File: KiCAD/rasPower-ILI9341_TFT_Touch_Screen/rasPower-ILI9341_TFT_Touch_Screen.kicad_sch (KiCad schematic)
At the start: 2 parts, among them J1 Raspberry_Pi_2_3, U2 ST7735_1.8"_TFT_128x160_w_SD-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

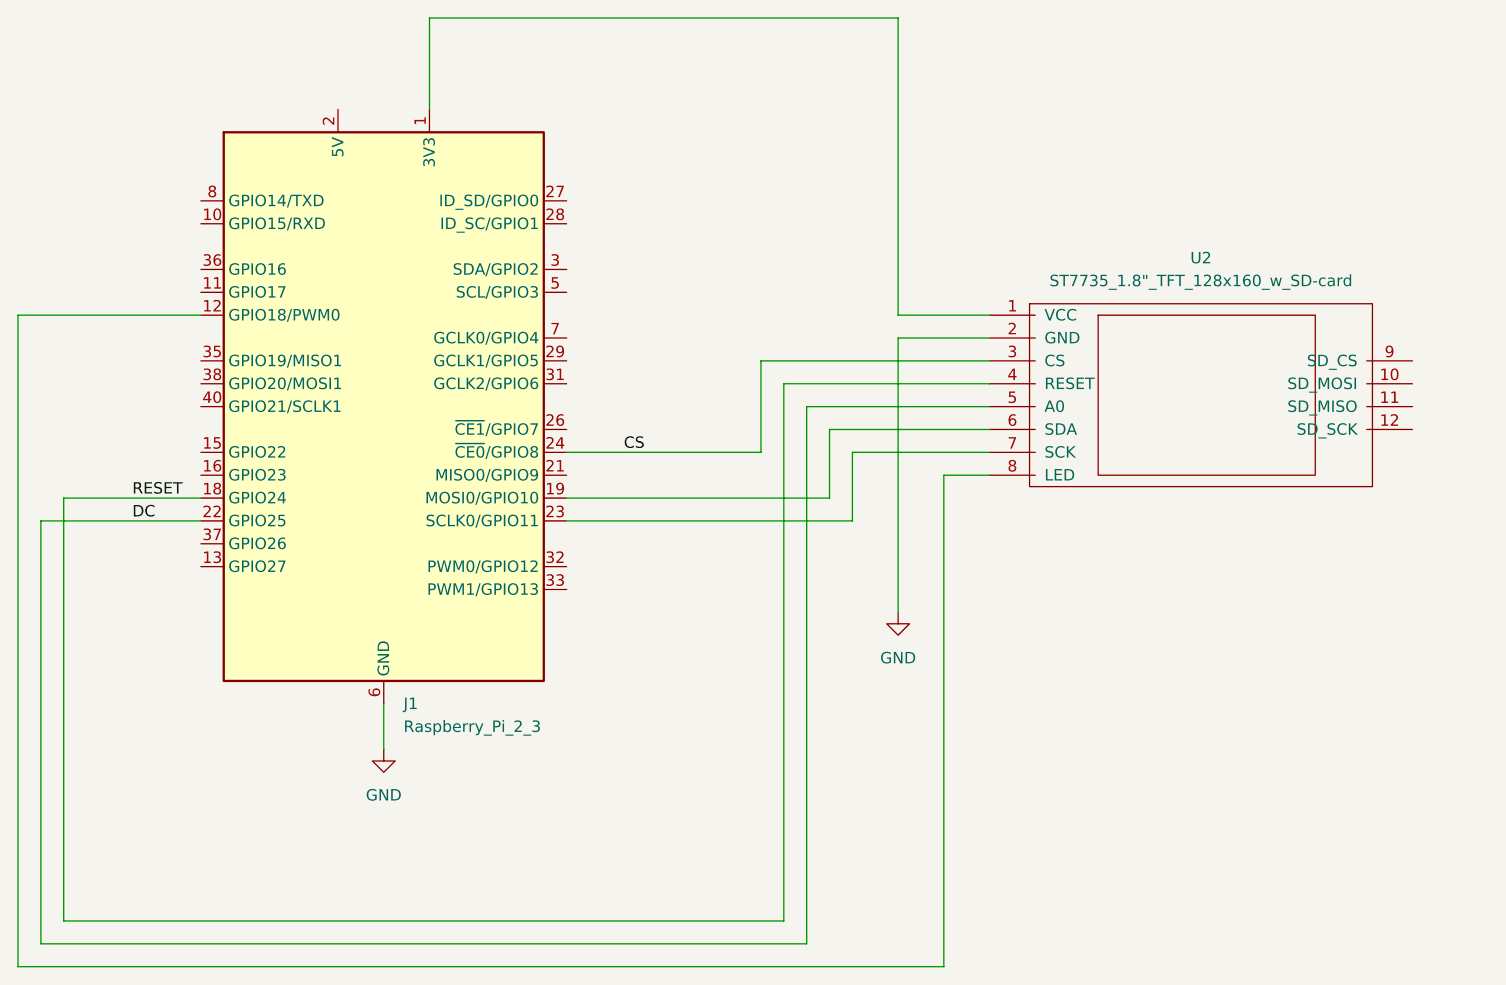
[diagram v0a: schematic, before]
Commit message: new ili9341 screen
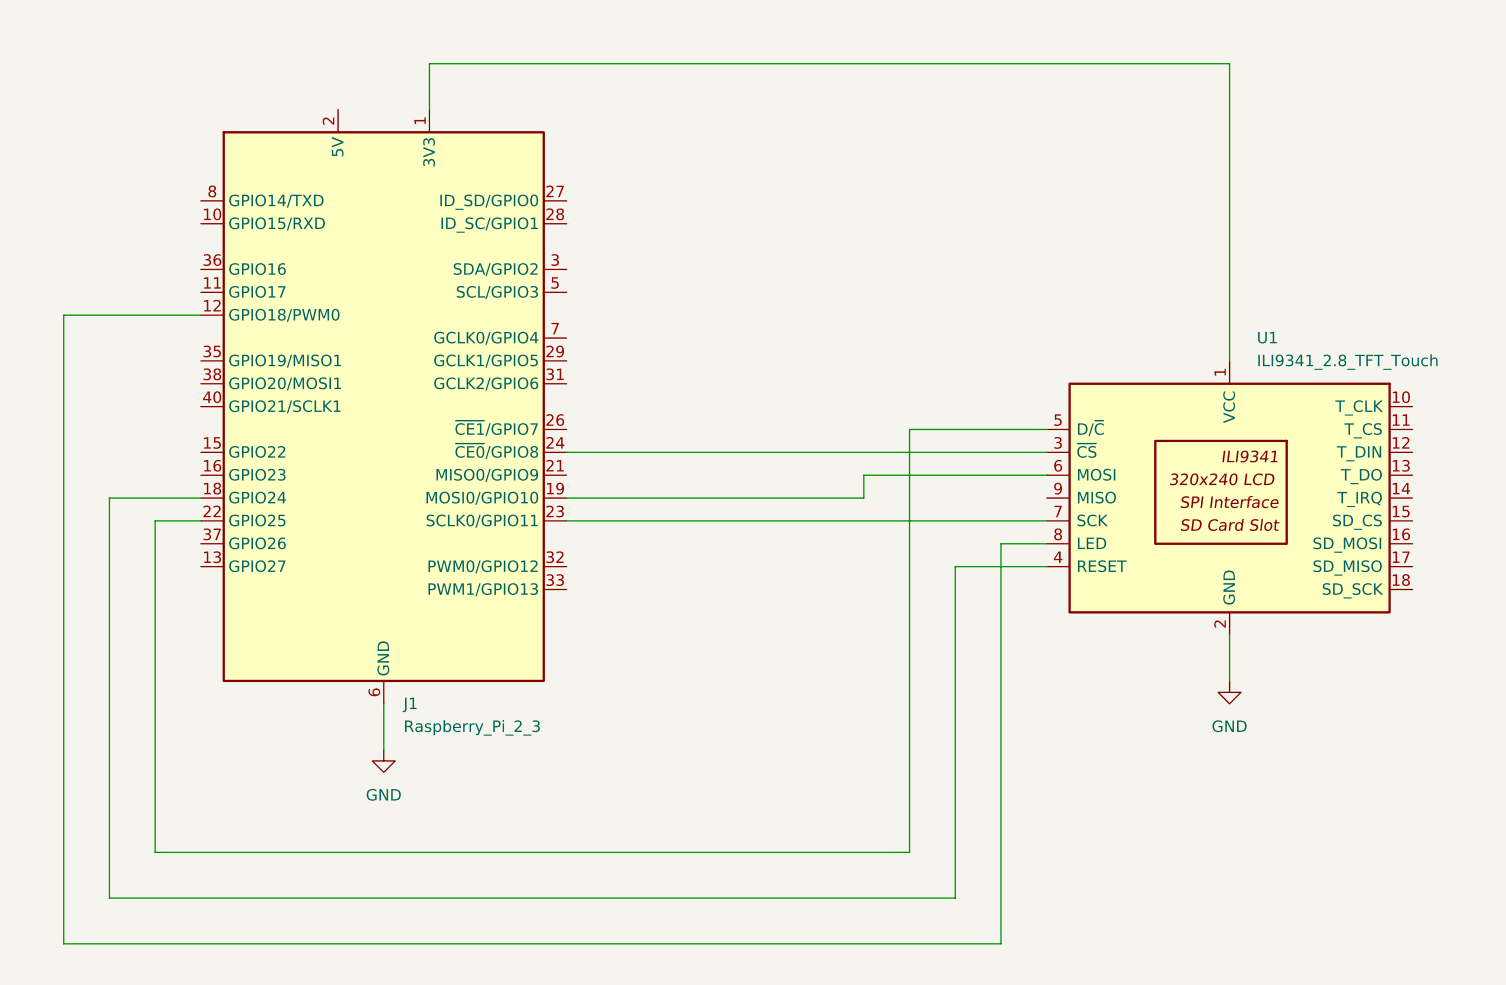
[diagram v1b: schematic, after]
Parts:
- removed U2: ST7735_1.8"_TFT_128x160_w_SD-card, symbol My_Parts:ST7735_1.8{dblquote}_TFT_128x160_w_SD-card
- added U1: ILI9341_2.8_TFT_Touch, My_Parts:ILI9341 2.8 TFT Touch large, symbol My_Symbols:ILI9341_2.8_TFT_Touch
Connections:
- net GND: now also U1.2 (GND)
- net at J1.1 (3V3), J1.17 (3V3): now also U1.1 (VCC)
- net at J1.12 (GPIO18/PWM0): now also U1.8 (LED)
- net at J1.19 (MOSI0/GPIO10): now also U1.6 (MOSI)
- net at J1.23 (SCLK0/GPIO11): now also U1.7 (SCK)
- net CS: no longer names the net of J1.24 (~{CE0}/GPIO8)
- net CS: now also U1.3 (~{CS})
- net DC: no longer names the net of J1.22 (GPIO25)
- net DC: now also U1.5 (D/~{C})
- net RESET: no longer names the net of J1.18 (GPIO24)
- net RESET: now also U1.4 (RESET)
